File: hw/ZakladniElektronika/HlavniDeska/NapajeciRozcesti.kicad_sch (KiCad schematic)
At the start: 28 parts, among them U13 TPS61088RHLR, U16 LD39200, U52 MCP1700x-180xxTT

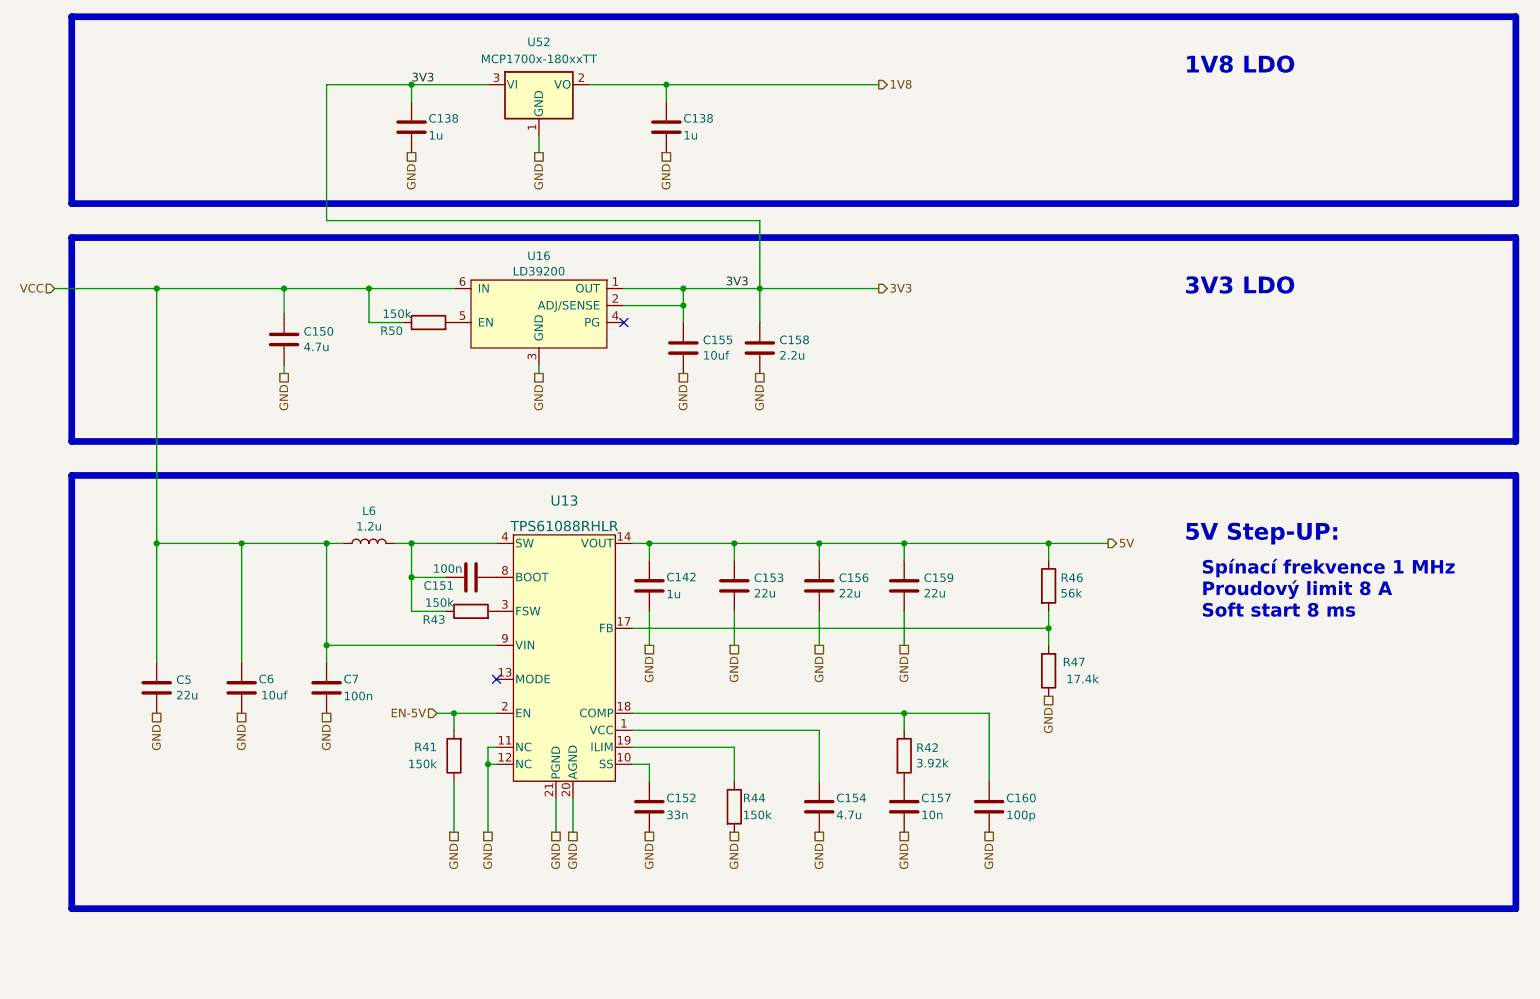
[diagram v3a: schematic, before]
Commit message: Likvidace MiniUI jako samostatné desky a výběr všech komponent
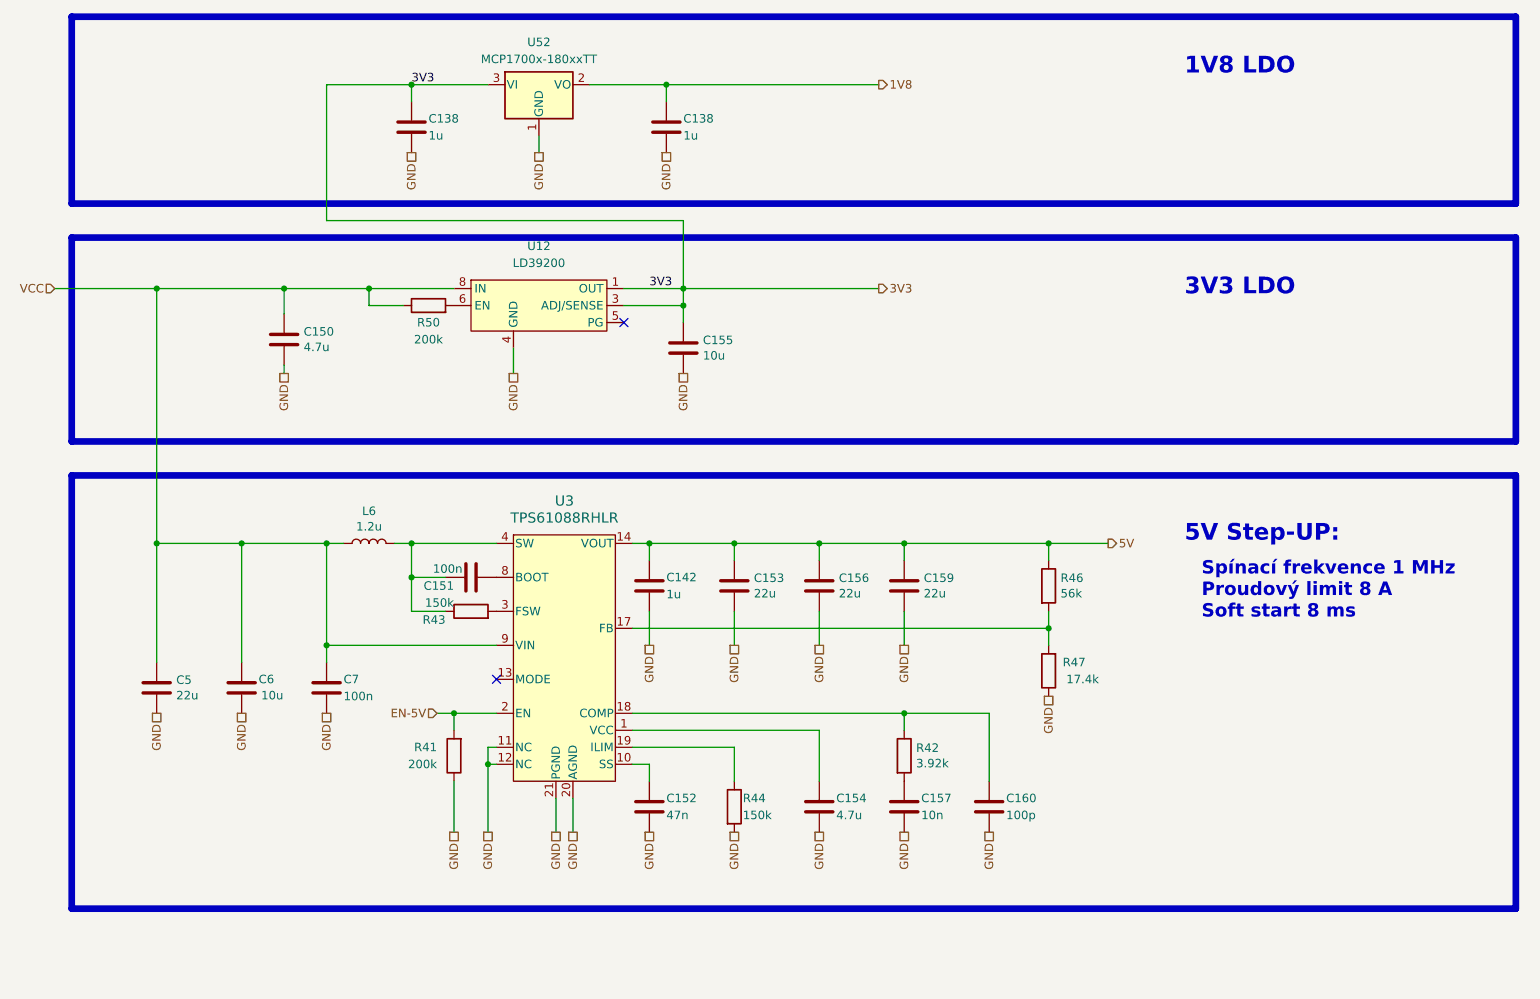
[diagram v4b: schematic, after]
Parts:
- removed C158: 2.2u, Capacitor_SMD:C_0805_2012Metric, symbol Device:C
- removed U13: TPS61088RHLR, RHL0020A, symbol Robotarna_KiCad_Library:TPS61088RHLR
- removed U16: LD39200, Package_DFN_QFN:DFN-6-1EP_3x3mm_P1mm_EP1.5x2.4mm, symbol B.B-rescue:LD39200-B.B-rescue
- added U12: LD39200, Package_DFN_QFN:DFN-8-1EP_4x4mm_P0.8mm_EP2.3x3.24mm, symbol RKL-LDO:LD39200
- added U3: TPS61088RHLR, RKL-StandardPackages:RHL0020A, symbol RKL-DcDcConverters:TPS61088RHLR
- C138: footprint Resistor_SMD:R_0402_1005Metric -> Capacitor_SMD:C_0402_1005Metric; Basic/Extended B -> E; JLCPCB_CORRECTION (none) -> 0;0;0; LCSC C52923 -> C1518208; info (none) -> 50V, X5R (potenciálně C52923 což je 25V, X5R )
- C142: info 50V, X7R -> 50V, X5R (potenciálně C52923 což je 25V, X5R )
- C150, C154: footprint Capacitor_SMD:C_0805_2012Metric -> Capacitor_SMD:C_0603_1608Metric; Basic/Extended (none) -> B; LCSC C1779 -> C19666; info (none) -> 16V, X5R
- C152: value 33n -> 47n; footprint Capacitor_SMD:C_0402_1005Metric -> Capacitor_SMD:C_0603_1608Metric; Basic/Extended (none) -> B; LCSC C1585 -> C1622; info (none) -> 50V, X7R
- C153, C156, C159, C5: Basic/Extended (none) -> B; info (none) -> 25V, X5R
- C155, C6: value 10uf -> 10u; footprint Capacitor_SMD:C_0805_2012Metric -> Capacitor_SMD:C_0603_1608Metric; Basic/Extended (none) -> B; LCSC C15850 -> C96446; info (none) -> 25V, X5R
- C157: Basic/Extended (none) -> B
- C160: Basic/Extended (none) -> B; info (none) -> 50V, C0G
- L6: footprint BB:MWSA0603_6.6x7.1x3.0 -> Inductor_SMD:L_Abracon_ASPI-0630LR; Basic/Extended (none) -> E
- R41, R50: value 150k -> 200k; Basic/Extended (none) -> B; LCSC C25755 -> C25764
- R42: Basic/Extended (none) -> E; LCSC C423178 -> C843949
- R43, R44: footprint Resistor_SMD:R_0402_1005Metric -> Resistor_SMD:R_0603_1608Metric; Basic/Extended (none) -> B; LCSC C25755 -> C22807
- R46: footprint Resistor_SMD:R_0402_1005Metric -> Resistor_SMD:R_0603_1608Metric; Basic/Extended (none) -> B; LCSC C25796 -> C23206
- R47, U52: Basic/Extended (none) -> E
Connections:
- net 3V3: now also U12.1 (OUT), U12.2 (OUT), U12.3 (ADJ/SENSE)
- net 5V: now also U3.14 (VOUT), U3.15 (VOUT), U3.16 (VOUT)
- net EN-5V: now also U3.2 (EN)
- net GND: now also U12.4 (GND), U12.9 (GND), U3.11 (NC), U3.12 (NC), U3.20 (AGND), U3.21 (PGND)
- net SW: now also U3.4 (SW), U3.5 (SW), U3.6 (SW), U3.7 (SW)
- net at C151.2: now also U3.8 (BOOT)
- net at R46.2, R47.2: now also U3.17 (FB)
- net at R44.1: now also U3.19 (ILIM)
- net at R50.2: now also U12.6 (EN)
- net at C160.1, R42.1: now also U3.18 (COMP)
- net at C154.1: now also U3.1 (VCC)
- net at R43.2: now also U3.3 (FSW)
- net at C152.1: now also U3.10 (SS)
- net VCC renamed IN
- net IN: now also U12.7 (IN), U12.8 (IN), U3.9 (VIN)
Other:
- moved on the sheet: R50

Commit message: Výmněna ochrany baterie
Předchozí ochranný čip JLCPCB nemělo na skladě
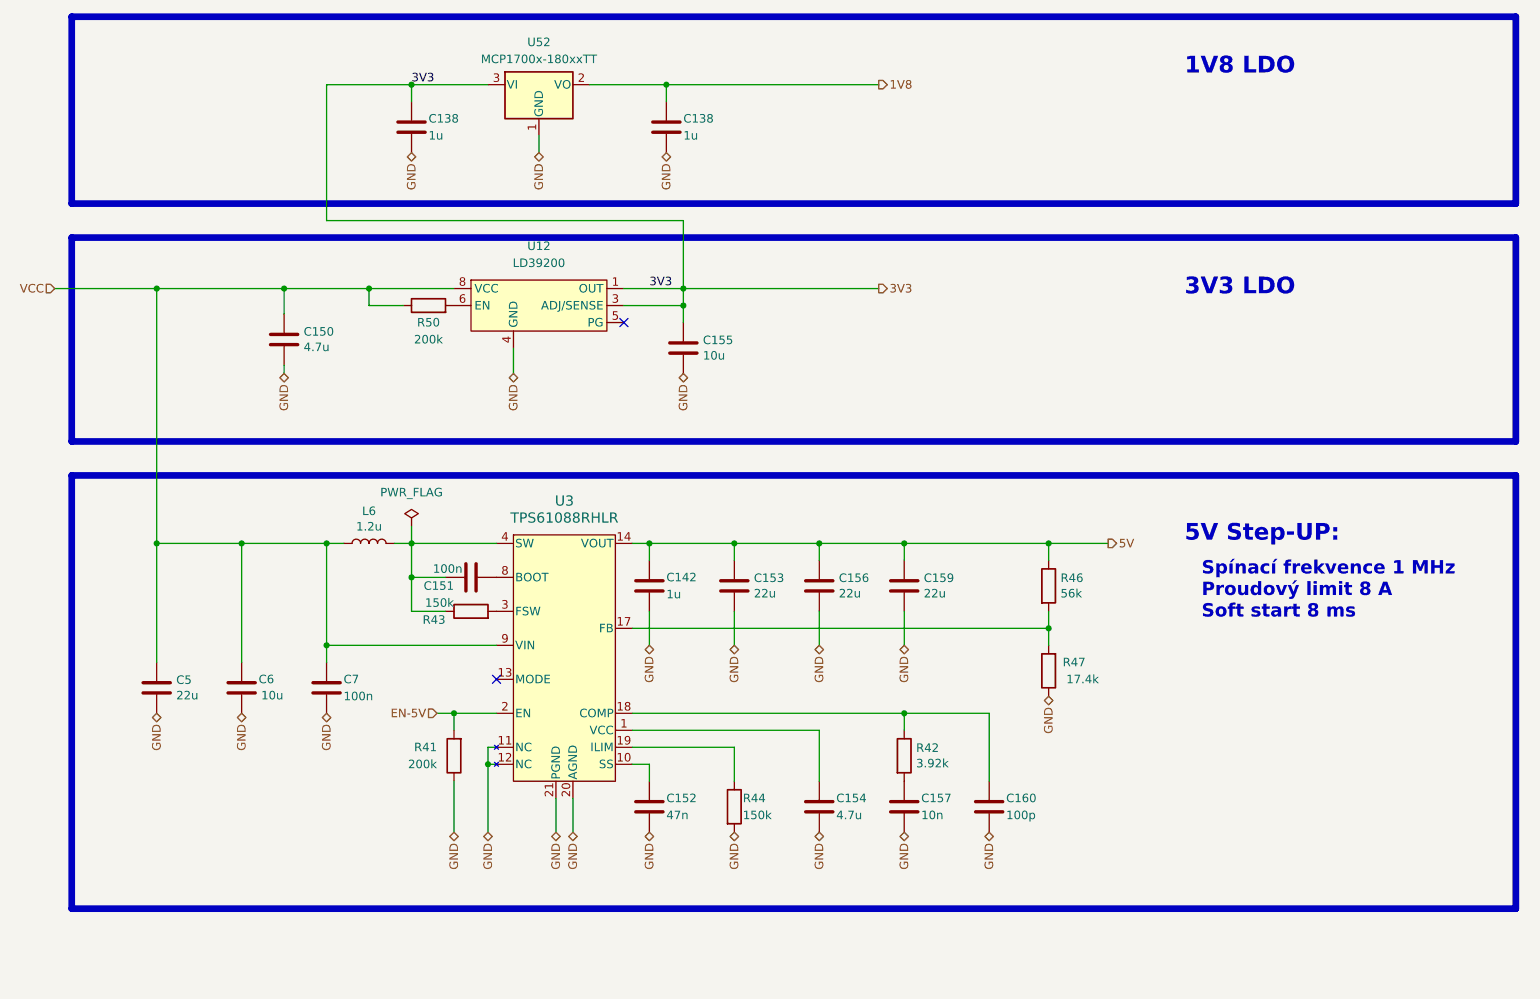
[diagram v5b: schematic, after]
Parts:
- L6: symbol B.B-rescue:L-Device-B.B-rescue-B.B-rescue -> Device:L
- R41, R42, R43, R44, R46, R47, R50: symbol B.B-rescue:R-Device-B.B-rescue-B.B-rescue -> Device:R
- U3: footprint RKL-StandardPackages:RHL0020A -> RHL0020A
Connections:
- net IN renamed VCC

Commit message: WIP
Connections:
- net GND: now also U3.0 (PGND)
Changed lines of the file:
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@@
     (pin "8")
     (pin "9")
+    (pin "0")
     (pin "11")
     (pin "12")

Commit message: AHS-V1
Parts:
- U12, U3: JLCPCB_CORRECTION (none) -> 0;0;-90
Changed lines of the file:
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@@
+      (effects (font (size 1.27 1.27)) hide)
+    )
+    (property "JLCPCB_CORRECTION" "0;0;-90" (at 111.76 97.79 0)
       (effects (font (size 1.27 1.27)) hide)
     )
@@
       (effects (font (size 1.27 1.27)) hide)
     )
+    (property "JLCPCB_CORRECTION" "0;0;-90" (at 107.95 59.69 0)
+      (effects (font (size 1.27 1.27)) hide)
+    )

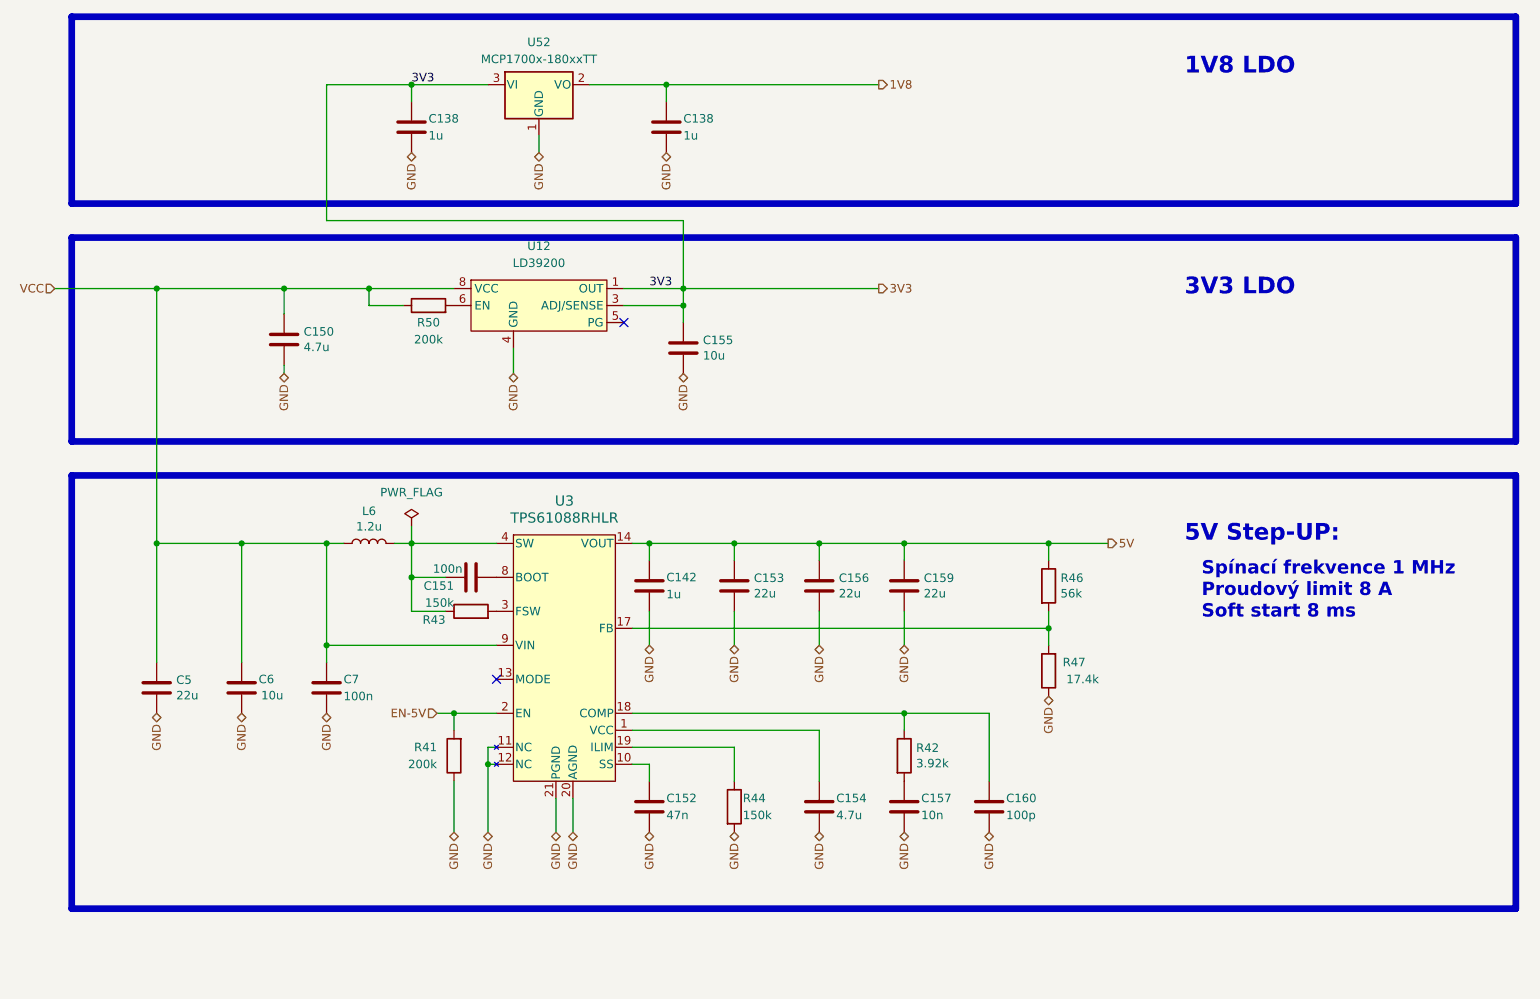
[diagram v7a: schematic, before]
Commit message: Řešení issue "Držák baterek" a " SemiSemafor V0"
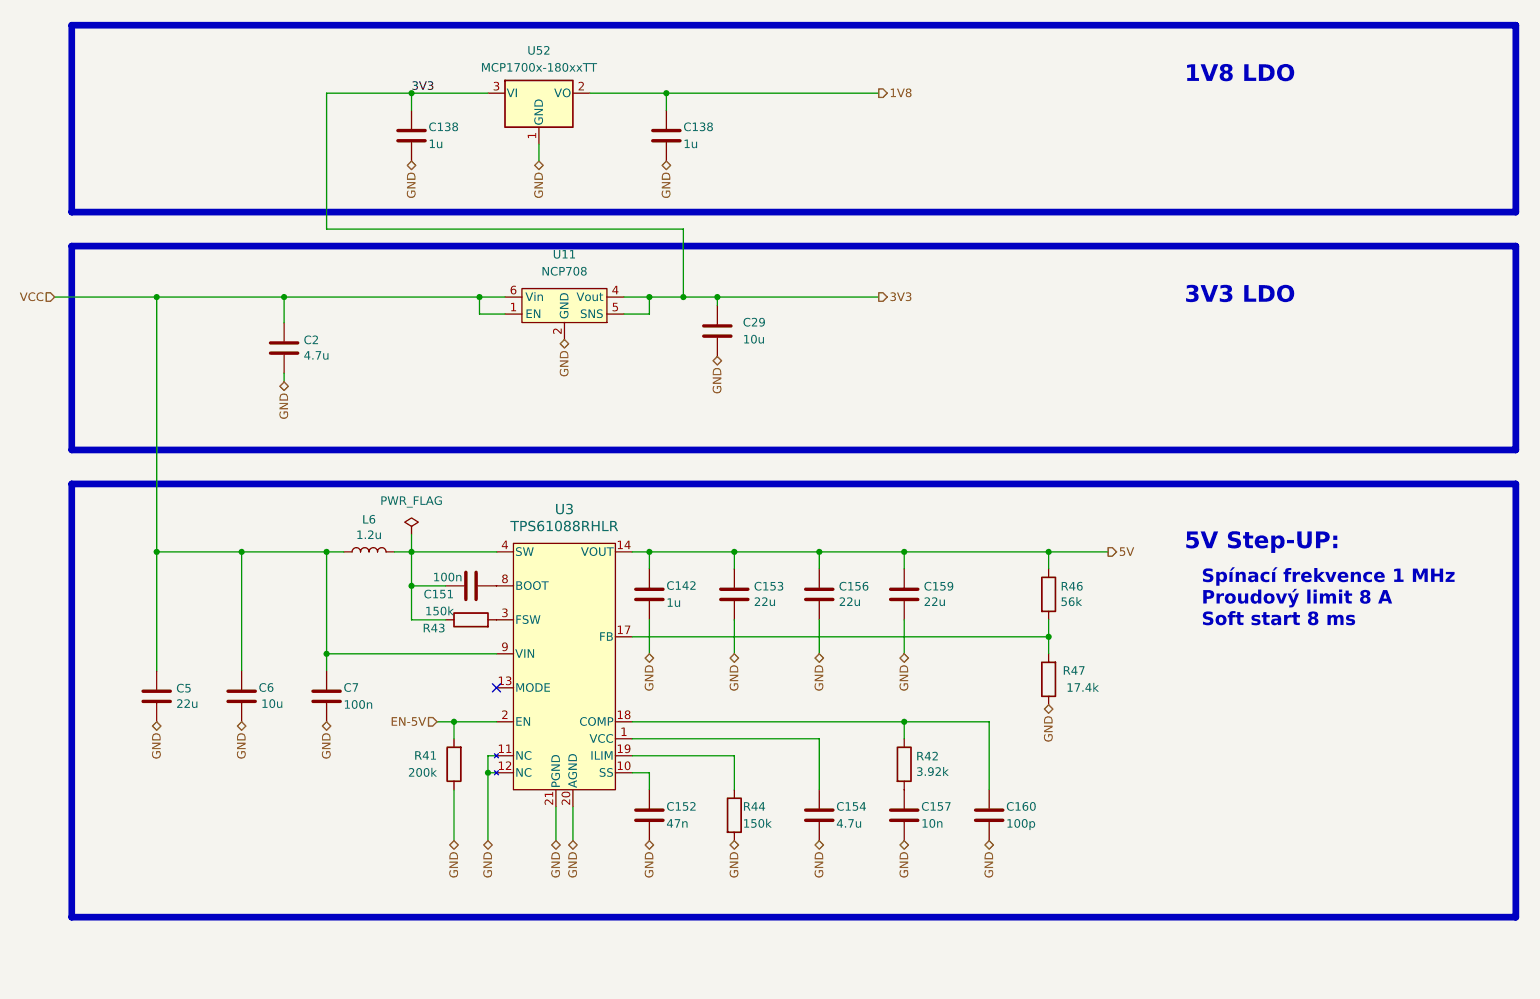
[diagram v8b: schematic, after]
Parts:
- removed C150: 4.7u, Capacitor_SMD:C_0603_1608Metric, symbol Device:C
- removed C155: 10u, Capacitor_SMD:C_0603_1608Metric, symbol Device:C
- removed R50: 200k, Resistor_SMD:R_0402_1005Metric, symbol Device:R
- removed U12: LD39200, Package_DFN_QFN:DFN-8-1EP_4x4mm_P0.8mm_EP2.3x3.24mm, symbol RKL-LDO:LD39200
- added C2: 4.7u, Capacitor_SMD:C_0603_1608Metric, symbol Device:C
- added C29: 10u, Capacitor_SMD:C_0603_1608Metric, symbol Device:C
- added U11: NCP708, RKL-StandardPackages:UDFN6-3x3mm, symbol RKL-LDO:NCP708
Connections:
- net 3V3: now also C29.1, U11.4 (Vout), U11.5 (SNS)
- net GND: now also C2.2, C29.2, U11.2 (GND), U11.7 (GND)
- net VCC: now also C2.1, U11.1 (EN), U11.6 (Vin)
- no-connect marks 2 -> 1
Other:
- moved on the sheet: C138, C142, C151, C152, C153, C154, C156, C157, C159, C160, C5, C6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
